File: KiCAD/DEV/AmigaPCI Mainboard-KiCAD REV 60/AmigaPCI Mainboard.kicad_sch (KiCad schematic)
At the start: 0 parts

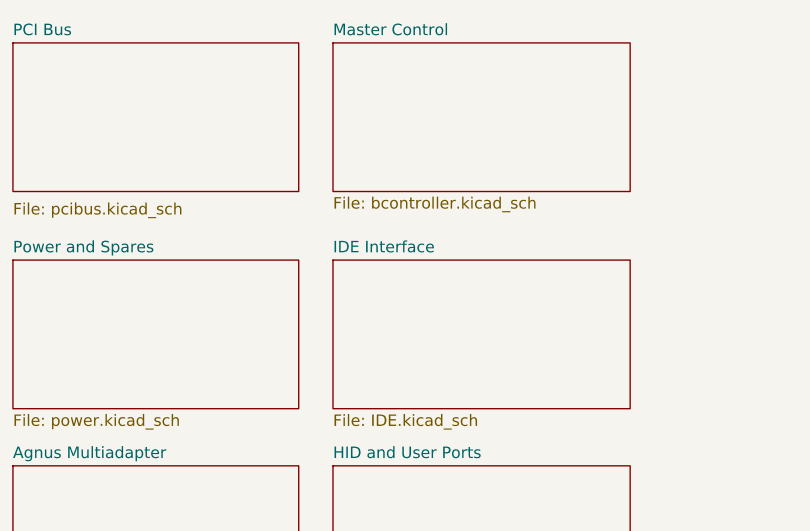
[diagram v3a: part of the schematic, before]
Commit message: Add flash and remove HID buffer.
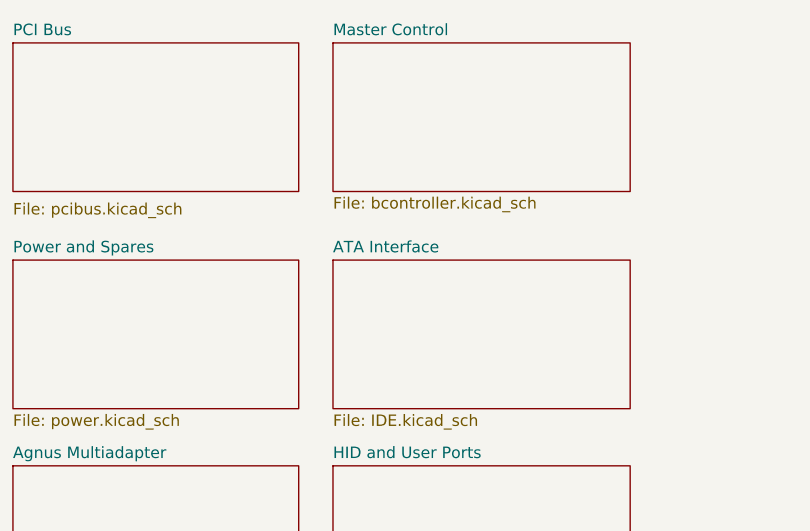
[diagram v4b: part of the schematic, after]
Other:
- sheet IDE Interface renamed ATA Interface
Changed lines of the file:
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@@
 	(title_block
 		(title "AMIGA PCI")
-		(date "2025-05-27")
+		(date "2025-06-26")
 		(rev "6.0")
 	)
@@
 			(color 0 0 0 0.0000)
 		)
-		(property "Sheetname" "IDE Interface"
+		(property "Sheetname" "ATA Interface"
 			(at 76.2 52.6284 0)
 			(effects
